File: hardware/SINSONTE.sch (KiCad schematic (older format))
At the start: 31 parts, among them J1 BAT, J10 Conn_01x01_Male, J11 Conn_01x01_Male, J12 Conn_01x04_Male, J13 Conn_01x01_Male, J14 Conn_01x02_Male, J2 CLOCK, J3 LIGHT_SENSOR, J4 Conn_01x17_Male, J5 Conn_01x01_Male, J6 Conn_01x01_Male, J7 Conn_01x01_Male, J8 Conn_01x01_Male, J9 PROG, Q1 2N7000, Q2 PN2222A, SW1 SW_Push, U1 Pico

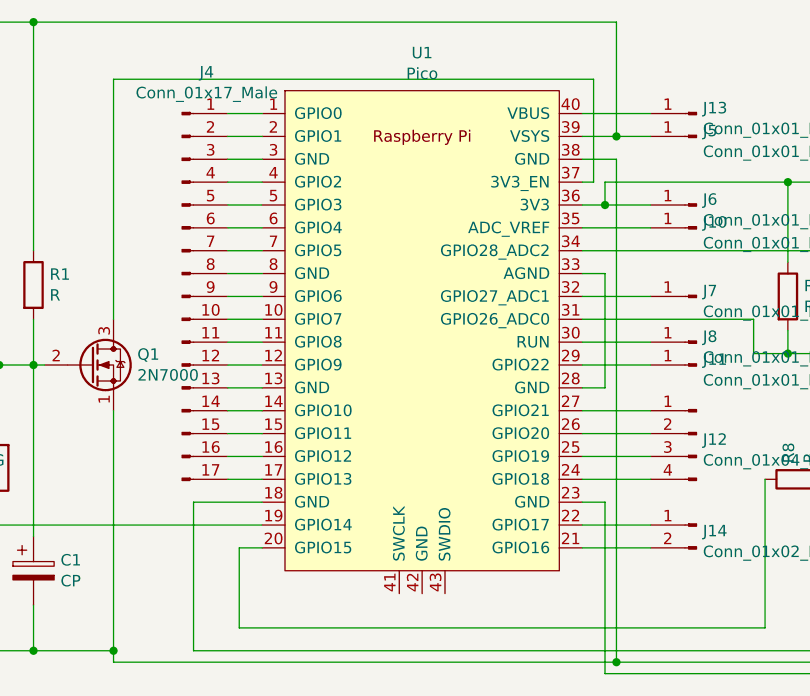
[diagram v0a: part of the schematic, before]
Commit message: copper ground plane, need some checks
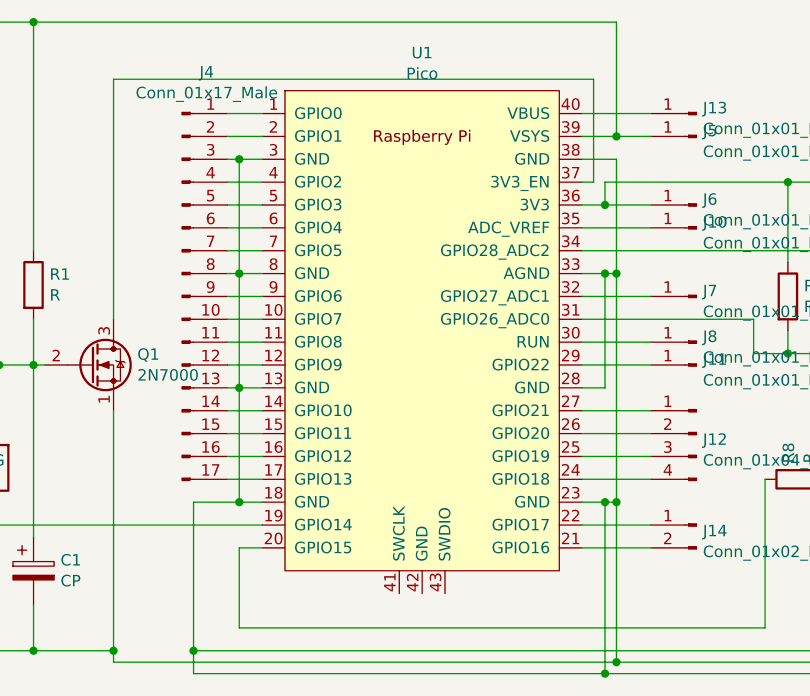
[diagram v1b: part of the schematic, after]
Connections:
- net at J4.13 (Pin_13), U1.13 (GND): now also BT1.2 (-), C1.2, C2.2, J1.2 (Pin_2), J3.2 (Pin_2), J4.3 (Pin_3), J4.8 (Pin_8), JP1.3 (B), Q1.1 (S), Q2.1 (E), R3.2, U1.18 (GND), U1.23 (GND), U1.28 (GND), U1.3 (GND), U1.33 (AGND), U1.38 (GND), U1.8 (GND)
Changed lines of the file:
@@
 	8250 3150 8300 3150
 Wire Wire Line
-	4900 4250 4600 4250
+	4900 4250 4800 4250
 Wire Wire Line
 	4900 4450 4800 4450
-Wire Wire Line
-	4800 4450 4800 4800
 Wire Wire Line
 	7100 4800 7100 4150
@@
 	4750 2650 4900 2650
 Wire Wire Line
-	4750 2750 4900 2750
+	4750 2750 4800 2750
 Wire Wire Line
 	4750 2850 4900 2850
@@
 	4750 3150 4900 3150
 Wire Wire Line
-	4750 3250 4900 3250
+	4750 3250 4800 3250
 Wire Wire Line
 	4750 3350 4900 3350
@@
 	4750 3650 4900 3650
 Wire Wire Line
-	4750 3750 4900 3750
+	4750 3750 4800 3750
 Wire Wire Line
 	4750 3850 4900 3850
@@
 	6300 3650 6600 3650
 Wire Wire Line
-	6450 2750 6450 4950
+	6450 2750 6450 3250
 $Comp
 L Connector:Conn_01x04_Male J12
@@
 Wire Wire Line
 	6300 4450 6600 4450
+Wire Wire Line
+	4800 2750 4800 3250
+Connection ~ 4800 2750
+Wire Wire Line
+	4800 2750 4900 2750
+Connection ~ 4800 3250
+Wire Wire Line
+	4800 3250 4900 3250
+Wire Wire Line
+	4800 3250 4800 3750
+Connection ~ 4800 3750
+Wire Wire Line
+	4800 3750 4900 3750
+Wire Wire Line
+	4800 3750 4800 4250
+Connection ~ 4800 4250
+Wire Wire Line
+	4800 4250 4600 4250
+Wire Wire Line
+	6400 3250 6450 3250
+Connection ~ 6400 3250
+Connection ~ 6450 3250
+Wire Wire Line
+	6450 3250 6450 4250
+Wire Wire Line
+	6400 4250 6450 4250
+Connection ~ 6400 4250
+Connection ~ 6450 4250
+Wire Wire Line
+	6450 4250 6450 4950
+Wire Wire Line
+	4800 4450 4800 4800
+Wire Wire Line
+	4600 4900 4600 5000
+Wire Wire Line
+	4600 5000 6400 5000
+Connection ~ 4600 4900
+Connection ~ 6400 5000
 $EndSCHEMATC

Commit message: changed transistors footprint for handsolder
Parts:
- Q1, Q2: footprint Package_TO_SOT_THT:TO-92_Inline -> Package_TO_SOT_THT:TO-92_HandSolder
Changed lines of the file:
@@
 F 0 "Q1" H 4354 3696 50  0000 L CNN
 F 1 "2N7000" H 4354 3605 50  0000 L CNN
-F 2 "Package_TO_SOT_THT:TO-92_Inline" H 4350 3575 50  0001 L CIN
+F 2 "Package_TO_SOT_THT:TO-92_HandSolder" H 4350 3575 50  0001 L CIN
 F 3 "https://www.fairchildsemi.com/datasheets/2N/2N7000.pdf" H 4150 3650 50  0001 L CNN
 	1    4150 3650
@@
 F 0 "Q2" H 9090 3196 50  0000 L CNN
 F 1 "PN2222A" H 9090 3105 50  0000 L CNN
-F 2 "Package_TO_SOT_THT:TO-92_Inline" H 9100 3075 50  0001 L CIN
+F 2 "Package_TO_SOT_THT:TO-92_HandSolder" H 9100 3075 50  0001 L CIN
 F 3 "http://www.fairchildsemi.com/ds/PN/PN2222A.pdf" H 8900 3150 50  0001 L CNN
 	1    8900 3150
@@
 $EndComp
 Wire Wire Line
-	6450 4950 8250 4950
-Wire Wire Line
 	4600 4900 7650 4900
 Wire Wire Line
@@
 	3750 3650 3900 3650
 Wire Wire Line
-	6450 4950 4250 4950
-Wire Wire Line
 	4250 4950 4250 4900
-Connection ~ 6450 4950
 Connection ~ 4250 4900
 Wire Wire Line
@@
 	6400 4250 6450 4250
 Connection ~ 6400 4250
-Connection ~ 6450 4250
-Wire Wire Line
-	6450 4250 6450 4950
 Wire Wire Line
 	4800 4450 4800 4800
@@
 Connection ~ 4600 4900
 Connection ~ 6400 5000
+Wire Wire Line
+	6450 4950 8250 4950
+Wire Wire Line
+	6450 4950 4250 4950
+Connection ~ 6450 4950
+Connection ~ 6450 4250
+Wire Wire Line
+	6450 4250 6450 4950
 $EndSCHEMATC

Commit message: program jumper trace minor update
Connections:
- net at J2.2 (Pin_2), J9.2 (Pin_2), R3.1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: now also J9.3 (Pin_3)
- no-connect marks 1 -> 0
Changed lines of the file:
@@
 Wire Wire Line
 	3000 4050 3000 4150
-NoConn ~ 3350 4100
 $Comp
 L Connector:Conn_01x02_Male J14
@@
 Wire Wire Line
 	6450 4250 6450 4950
+Wire Wire Line
+	3350 4100 3300 4100
+Wire Wire Line
+	3300 4100 3300 4050
+Connection ~ 3300 4050
 $EndSCHEMATC

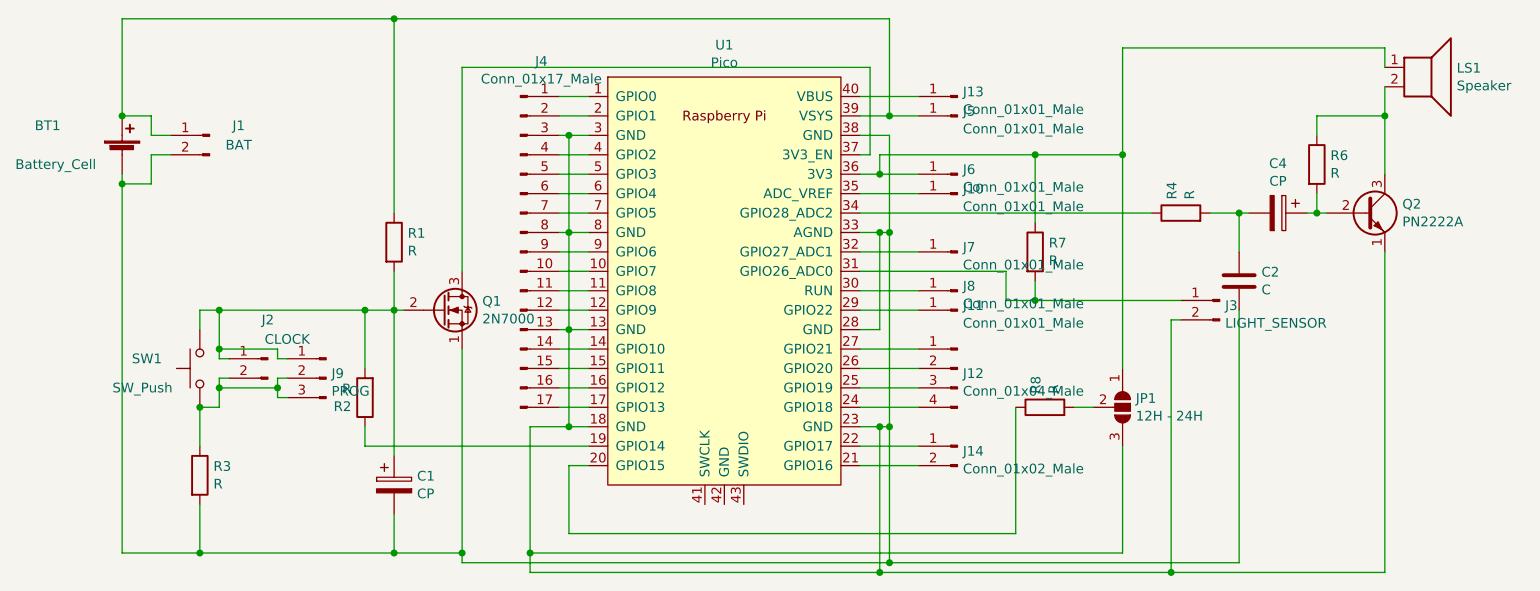
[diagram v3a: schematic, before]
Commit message: compontent values sch added
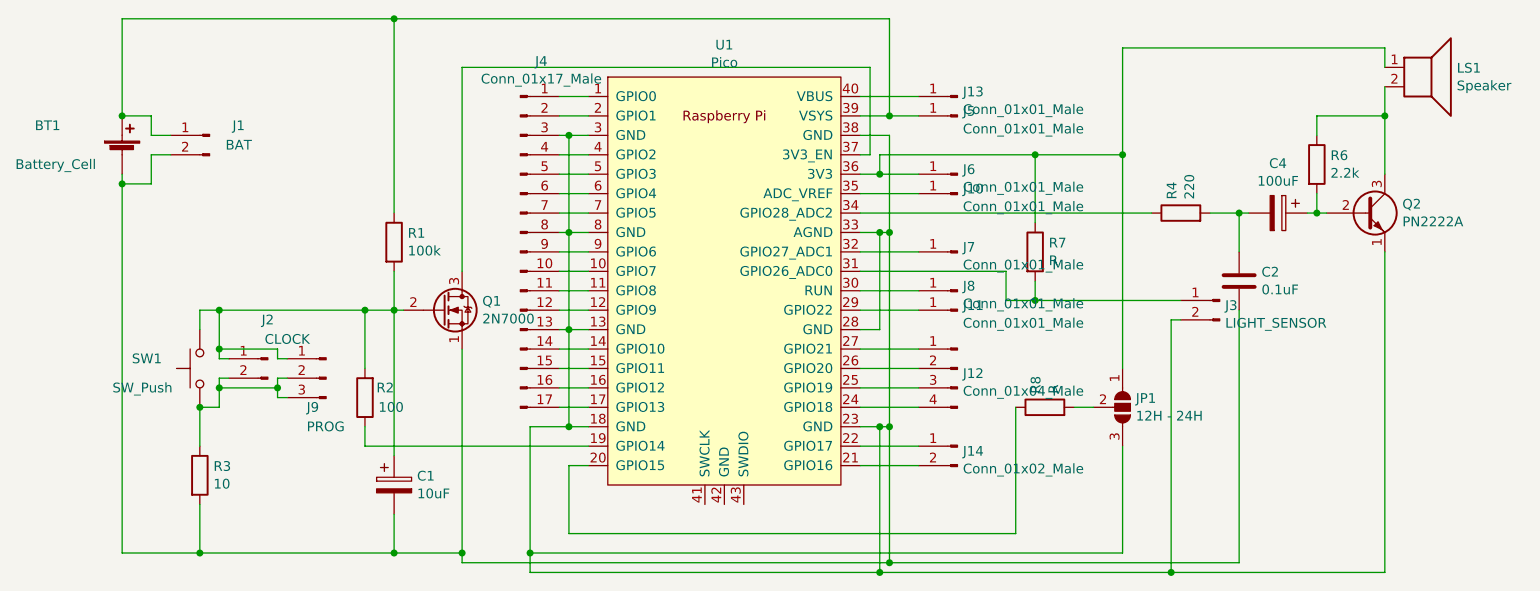
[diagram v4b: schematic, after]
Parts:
- C1: value CP -> 10uF
- C2: value C -> 0.1uF
- C4: value CP -> 100uF
- R1: value R -> 100k
- R2: value R -> 100
- R3: value R -> 10
- R4: value R -> 220
- R6: value R -> 2.2k
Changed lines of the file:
@@
 P 3900 3300
 F 0 "R1" H 3970 3346 50  0000 L CNN
-F 1 "R" H 3970 3255 50  0000 L CNN
+F 1 "100k" H 3970 3255 50  0000 L CNN
 F 2 "Resistor_THT:R_Axial_DIN0204_L3.6mm_D1.6mm_P2.54mm_Vertical" V 3830 3300 50  0001 C CNN
 F 3 "~" H 3900 3300 50  0001 C CNN
@@
 P 8250 3500
 F 0 "C2" H 8365 3546 50  0000 L CNN
-F 1 "C" H 8365 3455 50  0000 L CNN
+F 1 "0.1uF" H 8365 3455 50  0000 L CNN
 F 2 "Capacitor_THT:C_Disc_D5.0mm_W2.5mm_P5.00mm" H 8288 3350 50  0001 C CNN
 F 3 "~" H 8250 3500 50  0001 C CNN
@@
 P 7950 3150
 F 0 "R4" H 8020 3196 50  0000 L CNN
-F 1 "R" H 8020 3105 50  0000 L CNN
+F 1 "220" H 8020 3105 50  0000 L CNN
 F 2 "Resistor_THT:R_Axial_DIN0204_L3.6mm_D1.6mm_P2.54mm_Vertical" V 7880 3150 50  0001 C CNN
 F 3 "~" H 7950 3150 50  0001 C CNN
@@
 P 8450 3150
 F 0 "C4" V 8195 3150 50  0000 C CNN
-F 1 "CP" V 8286 3150 50  0000 C CNN
+F 1 "100uF" V 8286 3150 50  0000 C CNN
 F 2 "Capacitor_THT:CP_Radial_D6.3mm_P2.50mm" H 8488 3000 50  0001 C CNN
 F 3 "~" H 8450 3150 50  0001 C CNN
@@
 P 8650 2900
 F 0 "R6" H 8720 2946 50  0000 L CNN
-F 1 "R" H 8720 2855 50  0000 L CNN
+F 1 "2.2k" H 8720 2855 50  0000 L CNN
 F 2 "Resistor_THT:R_Axial_DIN0204_L3.6mm_D1.6mm_P2.54mm_Vertical" V 8580 2900 50  0001 C CNN
 F 3 "~" H 8650 2900 50  0001 C CNN
@@
 U 1 1 60464B9E
 P 3750 4100
-F 0 "R2" H 3820 4146 50  0000 L CNN
-F 1 "R" H 3820 4055 50  0000 L CNN
+F 0 "R2" H 3600 4050 50  0000 L CNN
+F 1 "100" H 3550 4150 50  0000 L CNN
 F 2 "Resistor_THT:R_Axial_DIN0204_L3.6mm_D1.6mm_P2.54mm_Vertical" V 3680 4100 50  0001 C CNN
 F 3 "~" H 3750 4100 50  0001 C CNN
@@
 P 2900 4500
 F 0 "R3" H 2970 4546 50  0000 L CNN
-F 1 "R" H 2970 4455 50  0000 L CNN
+F 1 "10" H 2970 4455 50  0000 L CNN
 F 2 "Resistor_THT:R_Axial_DIN0204_L3.6mm_D1.6mm_P2.54mm_Vertical" V 2830 4500 50  0001 C CNN
 F 3 "~" H 2900 4500 50  0001 C CNN
@@
 P 3900 4550
 F 0 "C1" H 4018 4596 50  0000 L CNN
-F 1 "CP" H 4018 4505 50  0000 L CNN
+F 1 "10uF" H 4018 4505 50  0000 L CNN
 F 2 "Capacitor_THT:CP_Radial_D6.3mm_P2.50mm" H 3938 4400 50  0001 C CNN
 F 3 "~" H 3900 4550 50  0001 C CNN
@@
 U 1 1 60882A91
 P 3550 4000
-F 0 "J9" H 3522 4024 50  0000 R CNN
-F 1 "PROG" H 3522 3933 50  0000 R CNN
+F 0 "J9" H 3650 3850 50  0000 R CNN
+F 1 "PROG" H 3650 3750 50  0000 R CNN
 F 2 "Connector_PinHeader_2.54mm:PinHeader_1x03_P2.54mm_Vertical" H 3550 4000 50  0001 C CNN
 F 3 "~" H 3550 4000 50  0001 C CNN

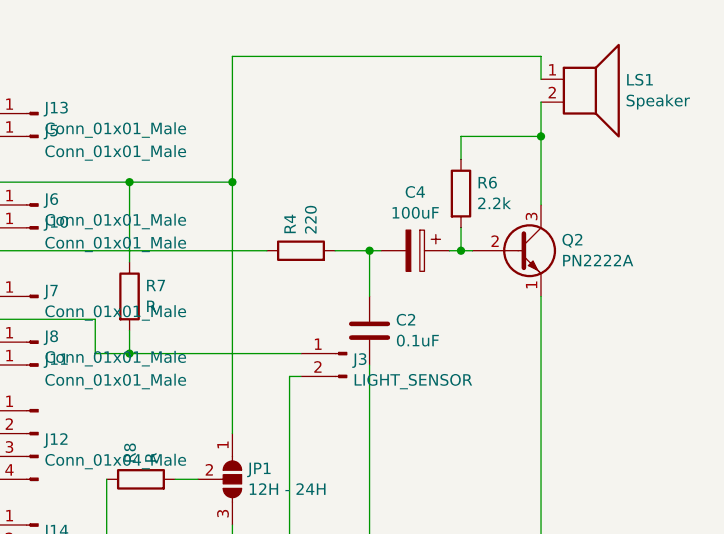
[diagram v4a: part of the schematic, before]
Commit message: capacitor fixed polarity
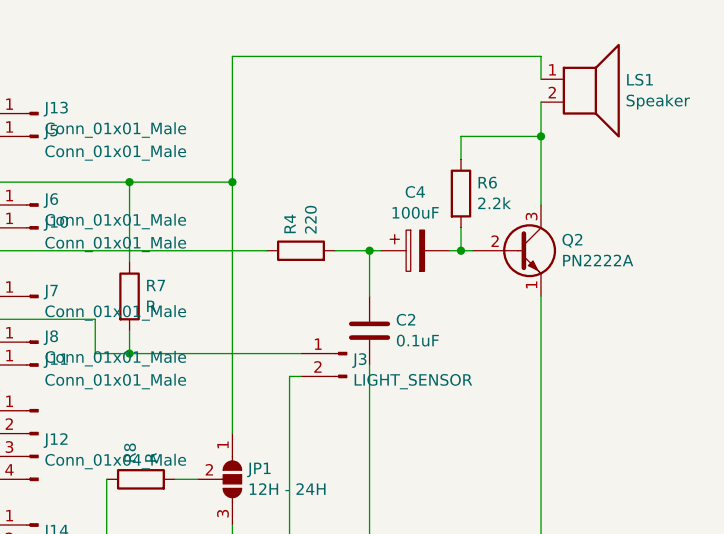
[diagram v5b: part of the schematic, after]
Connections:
- net at C2.1, R4.2: now also C4.1; no longer C4.2
- net at Q2.2 (B), R6.2: now also C4.2; no longer C4.1
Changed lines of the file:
@@
 Wire Wire Line
 	7800 3150 6300 3150
-Connection ~ 8250 3150
 $Comp
 L Device:CP C4
@@
 F 3 "~" H 8450 3150 50  0001 C CNN
 	1    8450 3150
-	0    1    1    0
+	0    -1   1    0
 $EndComp
 $Comp
@@
 $EndComp
 Wire Wire Line
-	8600 3150 8650 3150
-Wire Wire Line
 	8650 3050 8650 3150
-Connection ~ 8650 3150
 Wire Wire Line
 	8650 3150 8700 3150
@@
 	7400 4150 7500 4150
 Wire Wire Line
-	8250 3150 8300 3150
-Wire Wire Line
 	4900 4250 4800 4250
 Wire Wire Line
@@
 	3300 4100 3300 4050
 Connection ~ 3300 4050
+Wire Wire Line
+	8300 3150 8250 3150
+Connection ~ 8250 3150
+Wire Wire Line
+	8600 3150 8650 3150
+Connection ~ 8650 3150
 $EndSCHEMATC

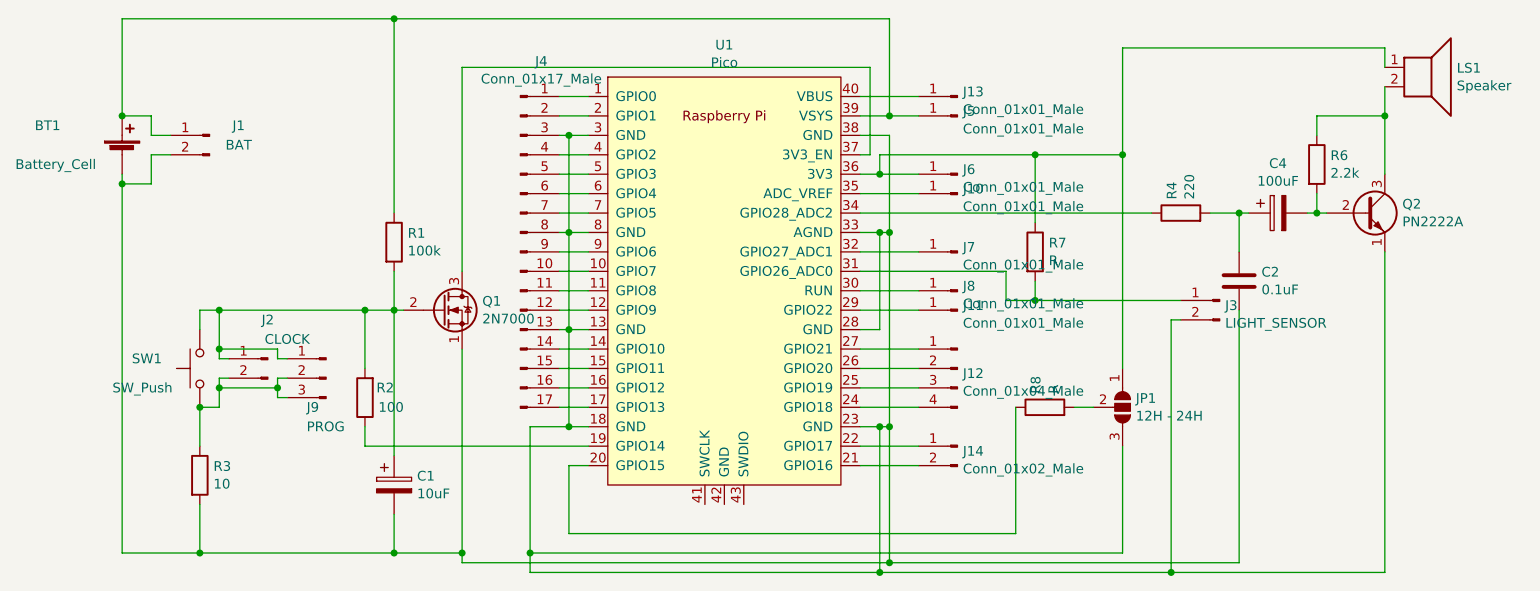
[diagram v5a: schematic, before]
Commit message: changed light sensor resistor to pull-down
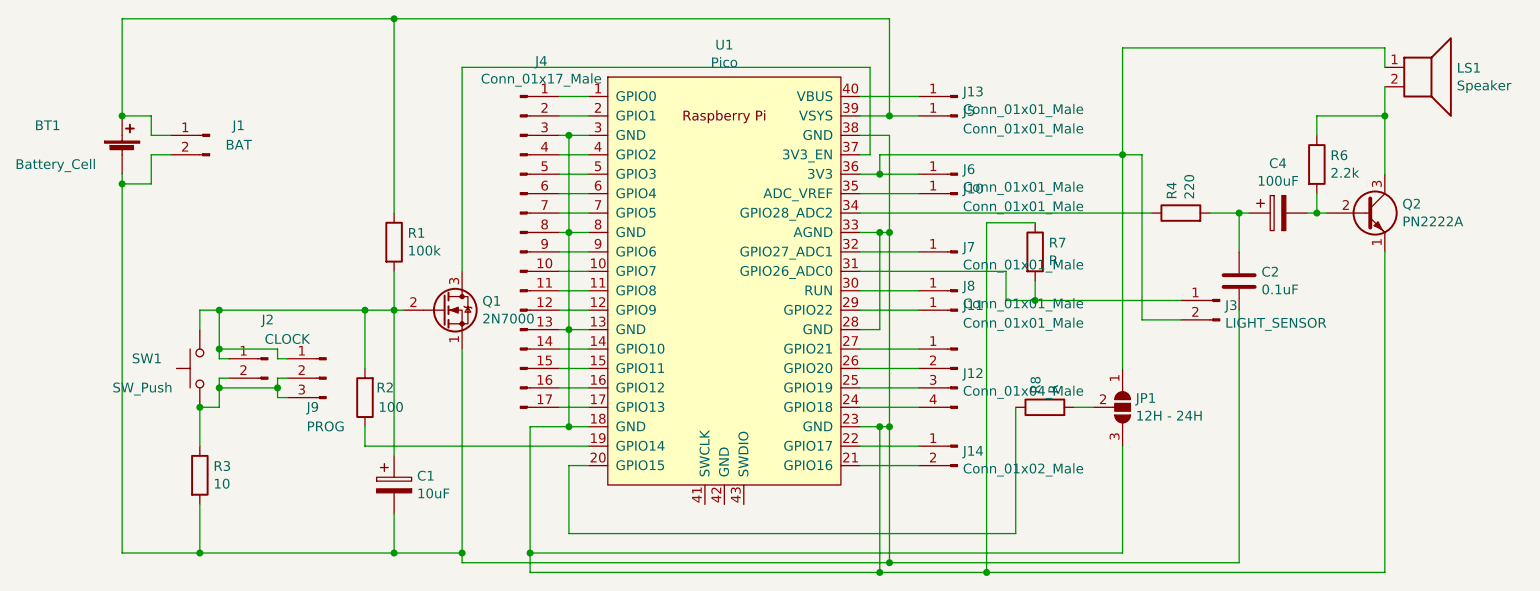
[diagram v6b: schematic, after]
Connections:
- net at BT1.2 (-), C1.2, C2.2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: now also R7.1; no longer J3.2 (Pin_2)
- net at J6.1 (Pin_1), JP1.1 (A), LS1.1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: now also J3.2 (Pin_2); no longer R7.1
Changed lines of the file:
@@
 $EndComp
-Wire Wire Line
-	7200 2850 7200 3200
 Wire Wire Line
 	6300 3450 7050 3450
@@
 	6400 4250 6400 5000
 Wire Wire Line
-	6400 5000 7900 5000
-Wire Wire Line
 	9000 3350 9000 5000
-Wire Wire Line
-	7950 3700 7900 3700
-Wire Wire Line
-	7900 3700 7900 5000
-Connection ~ 7900 5000
-Wire Wire Line
-	7900 5000 9000 5000
 $Comp
 L Connector:Conn_01x17_Male J4
@@
 	4600 4900 7650 4900
 Wire Wire Line
-	7200 2850 7650 2850
-Wire Wire Line
 	4800 4800 7100 4800
 Wire Wire Line
@@
 	7650 2850 7650 3950
 Wire Wire Line
-	7200 2850 6400 2850
-Wire Wire Line
 	6400 2950 6300 2950
-Connection ~ 7200 2850
 $Comp
 L Connector:Conn_01x01_Male J6
@@
 	8600 3150 8650 3150
 Connection ~ 8650 3150
+Wire Wire Line
+	6400 5000 6950 5000
+Wire Wire Line
+	7750 3700 7750 2850
+Wire Wire Line
+	7750 2850 7650 2850
+Wire Wire Line
+	7750 3700 7950 3700
+Wire Wire Line
+	6400 2850 7650 2850
+Wire Wire Line
+	7200 3200 6950 3200
+Wire Wire Line
+	6950 3200 6950 5000
+Connection ~ 6950 5000
+Wire Wire Line
+	6950 5000 9000 5000
 $EndSCHEMATC
